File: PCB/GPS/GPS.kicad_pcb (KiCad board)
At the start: 2 copper layers, 36 x 70 mm, 33 parts, among them J1 DC, J2 USB-C, J3 Shelly, J4 Conn_01x05_Male, J5 Conn_01x05_Male, U1 L86-M33, U2 ESP32-PICO-MINI-02, U3 FT231XQ, U4 LMR16006+FB, U5 QR

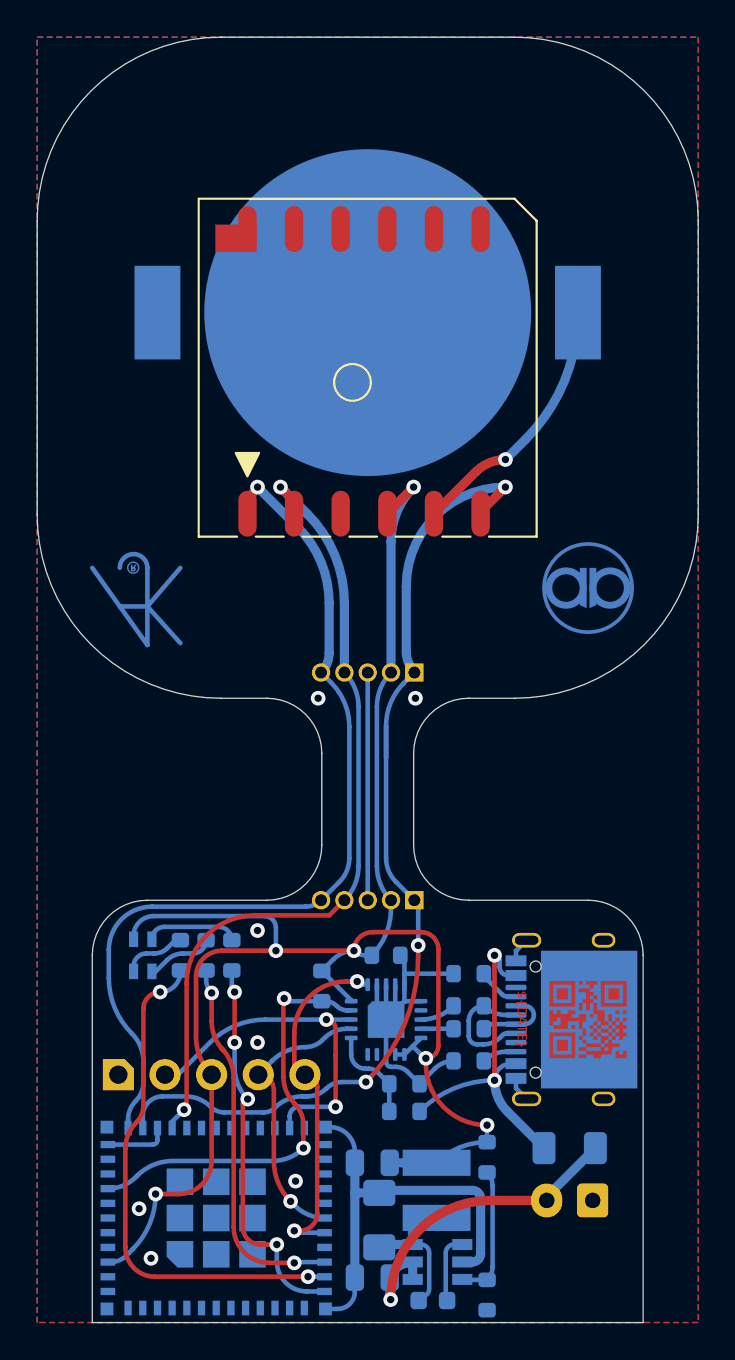
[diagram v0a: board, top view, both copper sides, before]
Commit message: Changed GPS to plug in module - will work with Generic when re-done
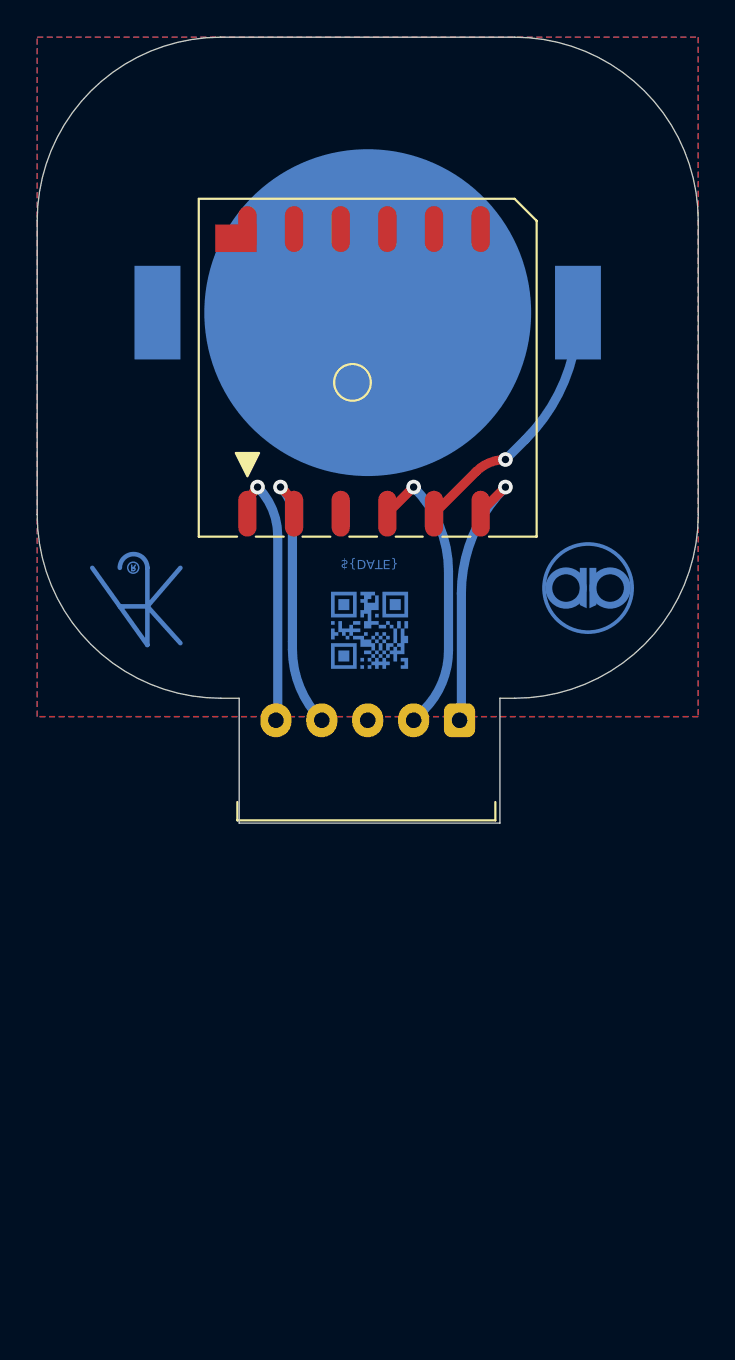
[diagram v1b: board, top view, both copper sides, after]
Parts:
- removed C1: 0.1uF, RevK:C_0603
- removed C2: 0.1uF, RevK:C_0603_
- removed C3: 2.2uF, RevK:C_0805_
- removed C4: 10uF, RevK:C_0805_
- removed D1: D, RevK:D_1206
- removed D2: LED_RGBA, RevK:LED-RGB-1.6x1.6
- removed D3: Schottky, RevK:D_1206_
- removed J2: USB-C, RevK:USC16-TR
- removed J3: Shelly, RevK:Shelly
- removed J4, J5: Conn_01x05_Male, Connector_PinHeader_1.27mm:PinHeader_1x05_P1.27mm_Vertical
- removed L1: 6.8uH, RevK:L_4x4_
- removed R1, R7: 10k, RevK:R_0603
- removed R10: 2K, RevK:R_0603
- removed R11: 220R, RevK:R_0603
- removed R12: 30k 1% or NF, RevK:R_0603
- removed R2, R3: 5K1, RevK:R_0603
- removed R4, R5: 27R, RevK:R_0603
- removed R6: 4k7, RevK:R_0603
- removed R8: 100k 1% or 0R, RevK:R_0603
- removed R9: 680R, RevK:R_0603
- removed U2: ESP32-PICO-MINI-02, RevK:ESP32-PICO-MINI-02
- removed U3: FT231XQ, RevK:QFN-20-1EP_4x4mm_P0.5mm_EP2.5x2.5mm
- removed U4: LMR16006+FB, RevK:SOT-23-Thin-6-Reg
- J1: value DC -> Conn_01x05; footprint RevK:Molex_MiniSPOX_H2RA -> RevK:PTSM-HH-5-RA-P; moved to F.Cu
- U5: moved to B.Cu
- moved J1 28.4 mm to (100.0, 119.2), turned to 0 degrees
- moved U5 24.3 mm to (100.1, 114.3), turned to 0 degrees
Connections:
- J1 pad 1: GND -> Net-(U1-Pad6)
- J1 pad 2: DC -> Net-(U1-Pad4)
- U1 pad 1: GPSRX -> Net-(U1-Pad1)
- U1 pad 2: GPSTX -> Net-(U1-Pad2)
- U1 pad 4: +3V3 -> Net-(U1-Pad4)
- U1 pad 6: TICK -> Net-(U1-Pad6)
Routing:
- net +3V3: track 96.6 -> 0.00 mm, vias 6 -> 0
- net TICK: track 54.9 -> 0.00 mm, vias 3 -> 0
- net GPSRX: track 49.8 -> 0.00 mm, vias 1 -> 0
- net GND: track 45.0 -> 0.00 mm, vias 7 -> 0
- net GPSTX: track 44.8 -> 0.00 mm, vias 2 -> 0
- net R: track 28.1 -> 0.00 mm, vias 2 -> 0
- net EN: track 23.5 -> 0.00 mm, vias 2 -> 0
- net B: track 21.1 -> 0.00 mm, vias 4 -> 0
- net G: track 20.7 -> 0.00 mm, vias 2 -> 0
- net BOOT: track 19.6 -> 0.00 mm, vias 2 -> 0
- net VBUS: track 19.6 -> 0.00 mm, vias 2 -> 0
- net O: track 19.5 -> 0.00 mm, vias 2 -> 0
- net DC: track 17.5 -> 0.00 mm, vias 1 -> 0
- net Net-(U1-Pad4): track 0.00 -> 15.8 mm, vias 0 -> 1
- net I: track 15.5 -> 0.00 mm, vias 1 -> 0
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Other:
- board size 36 x 70 mm -> 36 x 42.8 mm
- board text added: "->"
- board text added: "<-"
- board text added: "GND"
- board text added: "PPS"
- board text added: "VCC"
- board text removed: "DC 4V-60V"
- board text removed: "LED: 22/19/21"
- board text removed: "TX: 25 RX: 32 TICK: 33"

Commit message: New connectors, and separate GPS
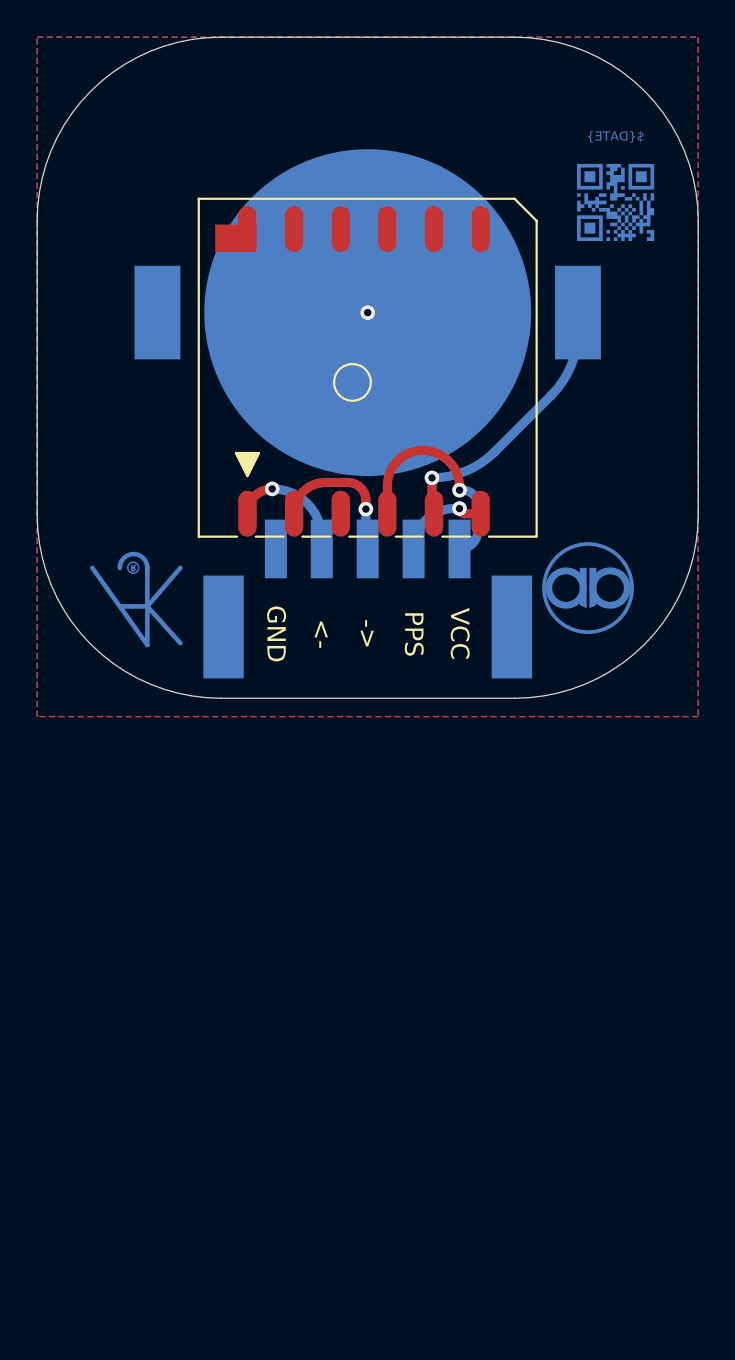
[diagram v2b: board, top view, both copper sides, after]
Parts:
- J1: footprint RevK:PTSM-HH-5-RA-P -> RevK:PTSM-HH-5-RA-P-SMD; moved to B.Cu
- moved U5 26.9 mm to (113.5, 91.0)
- moved J1 9.33 mm to (100.0, 109.9), turned to 180 degrees
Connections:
- J1 pad 1: Net-(U1-Pad6) -> GND
- J1 pad 2: Net-(U1-Pad4) -> Net-(J1-Pad2)
- J1 pad 3: GND -> Net-(J1-Pad3)
- J1 pad 4: Net-(U1-Pad2) -> Net-(J1-Pad4)
- J1 pad 5: Net-(U1-Pad1) -> Net-(J1-Pad5)
- U1 pad 1: Net-(U1-Pad1) -> Net-(J1-Pad2)
- U1 pad 2: Net-(U1-Pad2) -> Net-(J1-Pad3)
- U1 pad 4: Net-(U1-Pad4) -> Net-(J1-Pad5)
- U1 pad 6: Net-(U1-Pad6) -> Net-(J1-Pad4)
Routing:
- net Net-(U1-Pad4): track 15.8 -> 0.00 mm, vias 1 -> 0
- net Net-(U1-Pad6): track 15.3 -> 0.00 mm, vias 1 -> 0
- net Net-(U1-Pad2): track 14.9 -> 0.00 mm, vias 1 -> 0
- net Net-(U1-Pad1): track 14.6 -> 0.00 mm, vias 1 -> 0
- net Net-(J1-Pad5): track 0.00 -> 12.1 mm, vias 0 -> 1
- net Net-(J1-Pad3): track 0.00 -> 8.03 mm, vias 0 -> 1
- net Net-(J1-Pad2): track 0.00 -> 6.77 mm, vias 0 -> 1
- net Net-(J1-Pad4): track 0.00 -> 4.97 mm, vias 0 -> 1
- net BAT: track 14.2 -> 15.0 mm
- net GND: vias 0 -> 1
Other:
- board size 36 x 42.8 mm -> 36 x 36 mm

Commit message: Clean up
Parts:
- moved Logo2 26.0 mm to (114.0, 112.0), turned to 90 degrees
- moved Logo1 24.0 mm to (112.0, 88.0), turned to 90 degrees
- moved U5 14.6 mm to (114.0, 105.6), turned to 90 degrees
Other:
- board text added: "${CURRENT_DATE}"
- board text added: "<"
- board text added: ">"
- board text removed: "->"
- board text removed: "<-"

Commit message: Panel
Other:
- board text added: "⎍"
- board text removed: "PPS"

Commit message: Tidy
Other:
- board text added: "+"
- board text added: "⏚"
- board text removed: "GND"
- board text removed: "VCC"
